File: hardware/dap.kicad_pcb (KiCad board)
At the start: 4 copper layers, 60.8 x 105.8 mm, 158 parts, among them J1 Battery, J2 E-paper FPC, J3 Touch FPC, J4 USB-C, J5 microSD, J6 PJ-342, J7 4.4mm balanced, Q1 Si1308EDL, SW1 Play, SW2 Power, SW3 Vol+, SW4 Vol-, U1 BQ24073RGTR, U10 TUSB320LIRWBR, U11 FSUSB42MUX, U12 GL823K-HCY04, U13 TS3A27518EPWR, U14 SN74AVC4T774PWR, U15 PCA9306DCUR, U16 74LVC1G04, U17 CS43131-CNZR, U18 CS43131-CNZR, U2 TPS63001DRCR, U3 LP5907MFX-1.8, U4 LP5907MFX-1.8, U5 LP5907MFX-1.8, U6 TPS61023DRLR, U7 TPS2553DBVR, U8 ESP32-S3-WROOM-1-N16R8, U9 USBLC6-2SC6, Y1 22.5792MHz, Y2 24.576MHz

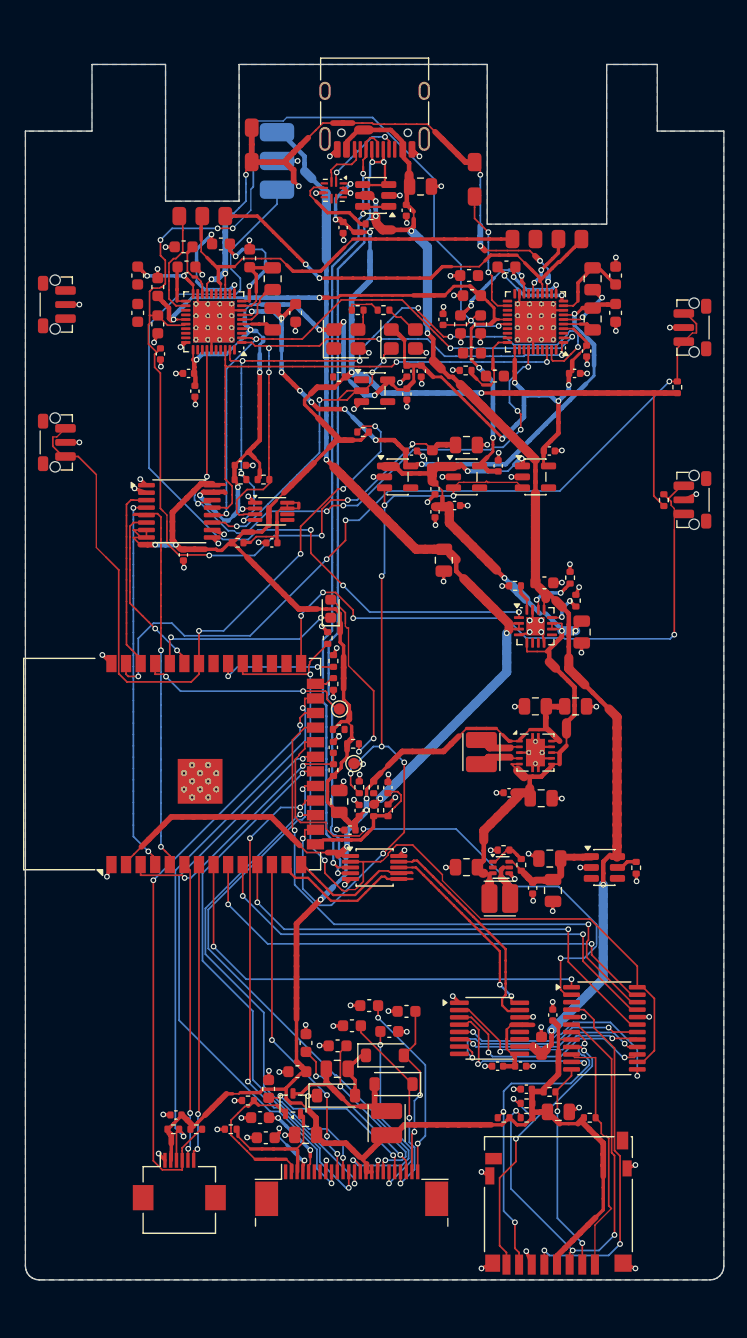
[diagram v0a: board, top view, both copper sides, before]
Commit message: Lengthen the board and case, hang both jacks under the board
The owner moved to a 5000 mAh 806090 cell (8 mm thick), and a 4.4 mm
jack turned out to be about 21 mm deep, not 14. Both headphone jacks now
hang from the back of the board into the top end, where the battery
isn't: the case is 65 x 116 x 17.2 mm and the board 60.8 x 111.8 mm.
Each port's hole is at its own part's height. The case check now also
looks for parts under the board that reach the battery or the back.

Footprints from the parts' drawings: the PJ-342 (SMD, two pegs), the
Kinghelm 4.4 mm jack (12 plated slots, a 1.15 mm notch so its nose ends
inside the case's face, and the cut-out its drawing asks for, with a
keep-out for the routers), and the TF-01A microSD socket. The e-paper
connector moves to x -0.4 mm, centred on the panel's ribbon as measured
on Good Display's drawing. The microSD moves to x 18.5 mm.

Routing is not finished: 32 connections are left in the audio area. The
clocks, level shifters and 1.8 V regulators now sit between the DACs, the
DACs keep a 1.4 mm ring free for their pins, Freerouting may also use
layer 3 (kept free under the USB pairs) and may redo all but the critical
nets, and its log, input and output are kept for another try.
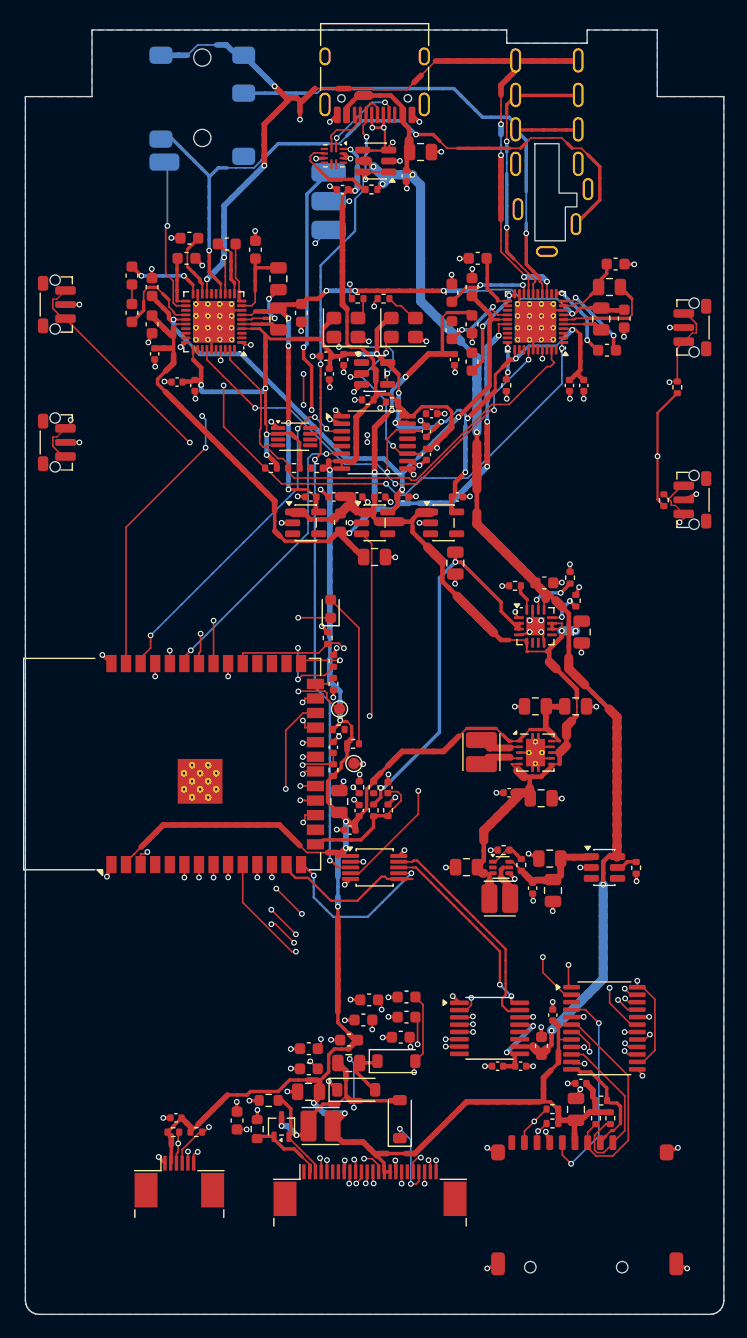
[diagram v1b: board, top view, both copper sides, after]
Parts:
- removed C79: 2.2uF, Capacitor_SMD:C_0603_1608Metric
- C34: value 1uF/50V -> 1uF; footprint Capacitor_SMD:C_0603_1608Metric -> Capacitor_SMD:C_0402_1005Metric
- C35: value 1uF -> 10uF; footprint Capacitor_SMD:C_0402_1005Metric -> Capacitor_SMD:C_0805_2012Metric
- C36, C44: value 10uF -> 100nF; footprint Capacitor_SMD:C_0805_2012Metric -> Capacitor_SMD:C_0402_1005Metric
- C39, C54, C68: value 100nF -> 4.7uF; footprint Capacitor_SMD:C_0402_1005Metric -> Capacitor_SMD:C_0603_1608Metric
- C40: value 4.7uF -> 1uF; footprint Capacitor_SMD:C_0603_1608Metric -> Capacitor_SMD:C_0402_1005Metric
- C41: value 1uF -> 100nF
- C43: value 100nF -> 10uF; footprint Capacitor_SMD:C_0402_1005Metric -> Capacitor_SMD:C_0805_2012Metric
- C55, C69: value 4.7uF -> 2.2uF
- C56, C70: value 2.2uF -> 22uF; footprint Capacitor_SMD:C_0603_1608Metric -> Capacitor_SMD:C_0805_2012Metric
- C57, C71: value 15uF -> 22uF
- C58, C72: value 15uF -> 2.2uF; footprint Capacitor_SMD:C_0805_2012Metric -> Capacitor_SMD:C_0603_1608Metric
- C65: value 2.2uF -> 100nF; footprint Capacitor_SMD:C_0603_1608Metric -> Capacitor_SMD:C_0402_1005Metric
- J3: footprint Connector_FFC-FPC:Hirose_FH12-6S-0.5SH_1x06-1MP_P0.50mm_Horizontal -> Connector_FFC-FPC:Jushuo_AFC07-S06FCA-00_1x6-1MP_P0.50_Horizontal
- J5: footprint Connector_Card:microSD_HC_Hirose_DM3D-SF -> dap:microSD_TF-01A
- J6: footprint dap:Jack_3.5mm_PJ-342_standin -> dap:Jack_3.5mm_PJ-342; moved to B.Cu
- J7: value 4.4mm balanced -> KH-PJ-44002-12DBAP-A; footprint dap:Jack_4.4mm_standin -> dap:Jack_4.4mm_KH-PJ-44002-12DBAP-A; moved to B.Cu
- R21: value 10k -> 1M; footprint Resistor_SMD:R_0402_1005Metric -> Resistor_SMD:R_0603_1608Metric
- R22: footprint Resistor_SMD:R_0402_1005Metric -> Resistor_SMD:R_0603_1608Metric
- R6: value 49.9k -> 47k
- moved C35 86.5 mm to (152.5, 59.7), turned to 0 degrees
- moved C45 55.9 mm to (153.0, 86.0), turned to -90 degrees
- moved C38 52.5 mm to (146.4, 118.7), turned to 180 degrees
- moved C65 38.8 mm to (165.5, 80.0), turned to -90 degrees
- moved C39 25.1 mm to (163.0, 137.5), turned to 90 degrees
- moved C46 23.7 mm to (153.0, 84.0), turned to 90 degrees
- moved C34 19.5 mm to (131.2, 143.8)
- moved C51 18.5 mm to (132.9, 80.0)
- moved U14 18.0 mm to (148.5, 85.0)
- moved C47 17.2 mm to (153.5, 82.5)
- moved C48 17.1 mm to (145.8, 77.8), turned to -90 degrees
- moved C14 12.6 mm to (148.5, 95.0)
- moved C55 12.5 mm to (142.1, 73.7)
- moved C69 12.5 mm to (170.2, 74.2)
- moved C67 11.5 mm to (155.5, 77.8)
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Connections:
- C29 pad 1: /Display/EPD_VPP -> /Display/EPD_VSH
- C30 pad 1: /Display/EPD_VSH -> /Display/EPD_PREVGH
- C31 pad 1: /Display/EPD_PREVGH -> /Display/EPD_VSL
- C32 pad 1: /Display/EPD_VSL -> /Display/EPD_PREVGL
- C33 pad 1: /Display/EPD_PREVGL -> /Display/EPD_VCOM
- C34 pad 1: /Display/EPD_VCOM -> +3V3
- C35 pad 1: +3V3 -> VBUS
- C37 pad 1: VBUS -> +3V3
- C39 pad 1: +3V3 -> VBUS
- C40 pad 1: VBUS -> GL_3V3
- C42 pad 1: GL_3V3 -> +3V3
- C46 pad 1: +3V3 -> 1V8_D
- C47 pad 1: 1V8_D -> /Audio/I2C_VREF2
- C48 pad 1: /Audio/I2C_VREF2 -> 1V8_D
- C53 pad 1: 1V8_D -> VP
- C55 pad 1: VP -> 1V8_A
- C56 pad 1: 1V8_A -> /Audio/DACL_FILTP
- C56 pad 2: GND -> 1V8_A
- C57 pad 1: /Audio/DACL_FILTP -> /Audio/DACL_FILTN
- C57 pad 2: 1V8_A -> /Audio/DACL_NVA
- C58 pad 1: /Audio/DACL_FILTN -> /Audio/DACL_NVA
- C58 pad 2: /Audio/DACL_NVA -> GND
- C59 pad 1: /Audio/DACL_NVA -> /Audio/DACL_FLYP_VA
- C59 pad 2: GND -> /Audio/DACL_FLYN_VA
- C60 pad 1: /Audio/DACL_FLYP_VA -> 1V8_CP
- C60 pad 2: /Audio/DACL_FLYN_VA -> GND
- C61 pad 1: 1V8_CP -> /Audio/DACL_VCPF_P
- C62 pad 1: /Audio/DACL_VCPF_P -> /Audio/DACL_VCPF_N
- C63 pad 1: /Audio/DACL_VCPF_N -> /Audio/DACL_FLYP_VCP
- C63 pad 2: GND -> /Audio/DACL_FLYC_VCP
- C64 pad 1: /Audio/DACL_FLYP_VCP -> /Audio/DACL_FLYC_VCP
- C64 pad 2: /Audio/DACL_FLYC_VCP -> /Audio/DACL_FLYN_VCP
- C65 pad 1: /Audio/DACL_FLYC_VCP -> 1V8_D
- C65 pad 2: /Audio/DACL_FLYN_VCP -> GND
- C67 pad 1: 1V8_D -> VP
- C69 pad 1: VP -> 1V8_A
- C70 pad 1: 1V8_A -> /Audio/DACR_FILTP
- C70 pad 2: GND -> 1V8_A
- C71 pad 1: /Audio/DACR_FILTP -> /Audio/DACR_FILTN
- C71 pad 2: 1V8_A -> /Audio/DACR_NVA
- C72 pad 1: /Audio/DACR_FILTN -> /Audio/DACR_NVA
- C72 pad 2: /Audio/DACR_NVA -> GND
- C73 pad 1: /Audio/DACR_NVA -> /Audio/DACR_FLYP_VA
- C73 pad 2: GND -> /Audio/DACR_FLYN_VA
- C74 pad 1: /Audio/DACR_FLYP_VA -> 1V8_CP
- C74 pad 2: /Audio/DACR_FLYN_VA -> GND
- C75 pad 1: 1V8_CP -> /Audio/DACR_VCPF_P
- C76 pad 1: /Audio/DACR_VCPF_P -> /Audio/DACR_VCPF_N
- C77 pad 1: /Audio/DACR_VCPF_N -> /Audio/DACR_FLYP_VCP
- C77 pad 2: GND -> /Audio/DACR_FLYC_VCP
- C78 pad 1: /Audio/DACR_FLYP_VCP -> /Audio/DACR_FLYC_VCP
- C78 pad 2: /Audio/DACR_FLYC_VCP -> /Audio/DACR_FLYN_VCP
- J2 pad 19: /Display/EPD_VPP -> unconnected-(J2-Pin_19-Pad19)
- J6 pad 3: /Audio/OUT_RP -> /Audio/OUT_LP
- J6 pad 4: /Audio/OUT_LP -> /Audio/DET_35
- J6 pad 5: /Audio/DET_35 -> /Audio/HP_GND
- J7 pad 1: /Audio/OUT_LP -> /Audio/HP_GND
- J7 pad 2: /Audio/OUT_LN -> /Audio/OUT_RN
- J7 pad 4: /Audio/OUT_RN -> /Audio/OUT_LN
- J7 pad 5: /Audio/HP_GND -> /Audio/OUT_LP
- J7 pad 6: /Audio/DET_44 -> /Audio/HP_GND
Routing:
- net /MCU/KEY_VOLUP: track 0.00 -> 55.3 mm, vias 0 -> 3
- net /Audio/SDIN_1V8: track 50.8 -> 0.00 mm, vias 4 -> 0
- net AUDIO_EN: track 68.9 -> 23.8 mm, vias 8 -> 2
- net /Audio/LRCK_1V8: track 44.8 -> 0.00 mm, vias 2 -> 0
- net /Audio/MCLK: track 3.05 -> 41.5 mm, vias 0 -> 4
- net +3V3: track 294.3 -> 256.9 mm
- net I2S_SDOUT: track 34.3 -> 0.00 mm, vias 2 -> 0
- net I2S_LRCK: track 33.0 -> 0.00 mm, vias 2 -> 0
- net VP: track 119.4 -> 88.8 mm, vias 9 -> 7
- net /Audio/HP_GND: track 57.0 -> 86.2 mm, vias 7 -> 8
- net /USB and storage/USB_DM: track 74.2 -> 101.7 mm, vias 3 -> 4
- net /Power/BAT_NTC: track 72.3 -> 45.0 mm, vias 3 -> 6
- net /Audio/OUT_LP: track 35.2 -> 60.4 mm, vias 0 -> 2
- net /USB and storage/SDC_CMD: track 41.1 -> 19.2 mm, vias 3 -> 0
- net /Audio/OUT_RN: track 5.67 -> 24.2 mm
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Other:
- board size 60.8 x 105.8 mm -> 60.8 x 111.8 mm
- board text added: "E-ink DAP v0.1 2026-10-31"
- board text removed: "E-ink DAP v0.1 draft 2026-10-26"

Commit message: Route the board on 6 layers
The board is now top, ground, signal, signal, ground, bottom, and every
net is routed with KiCad's DRC clean.

- Our router routes every net. Its search is guided by the true distance
  through free space (Dijkstra over the window), so long connections no
  longer run out of steps.
- Each fine-pitch pin, every FPC connector pin and every ESP32 pin gets an
  escape stub and a via of its own before routing, so nothing can wall it
  in. A pin with no room takes back its neighbours' vias.
- Rip-up is a trial: kept only if fewer connections are left, otherwise
  put back exactly. It may also move neighbouring pins' vias.
- DAC capacitors that sit between two pins of their chip are placed
  first, with a 0.6 mm ring and a free strip at the charge-pump pins.
- Freerouting only adds to our fixed tracks, and is skipped when nothing
  is left. Dead-end removal can no longer cut a connection, and a repair
  step judged by KiCad's own count closes anything still open.
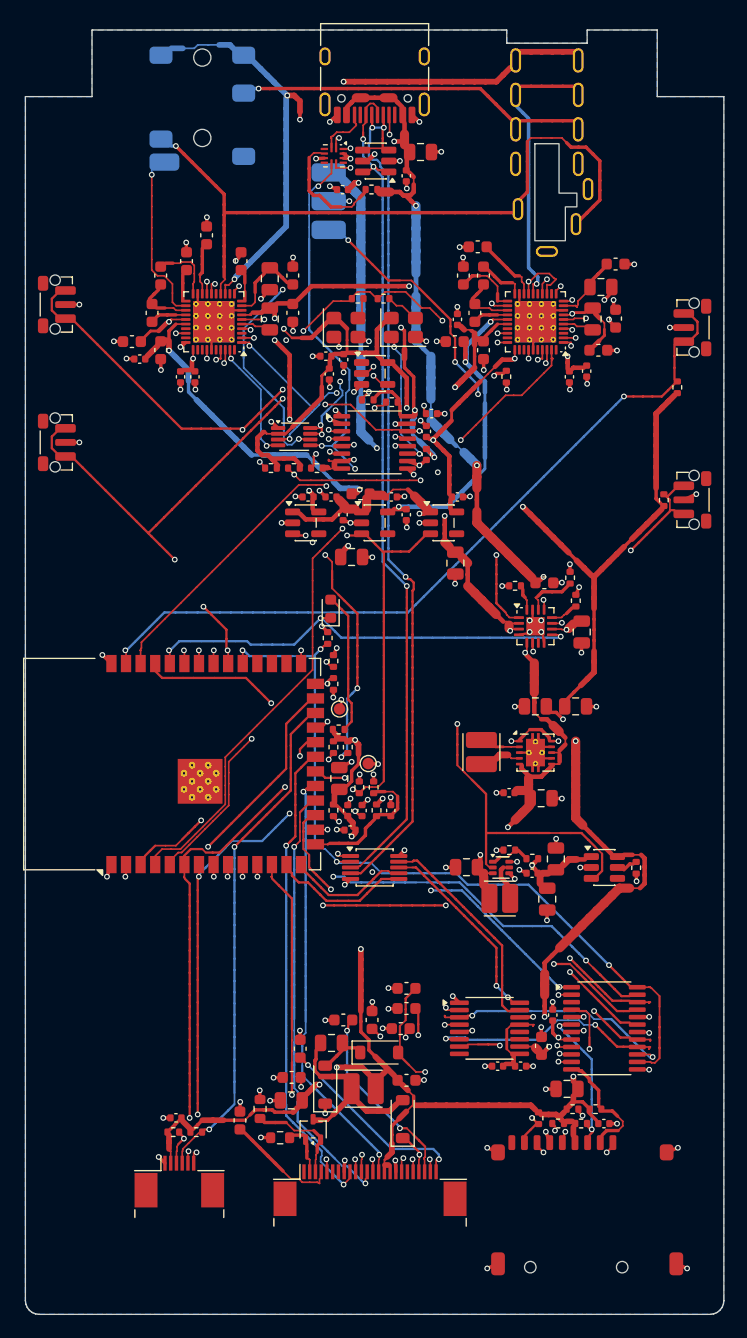
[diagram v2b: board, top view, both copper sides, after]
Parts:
- moved C78 7.57 mm to (158.0, 70.5), turned to 90 degrees
- moved C33 7.35 mm to (142.0, 137.8), turned to 90 degrees
- moved C27 6.10 mm to (151.3, 140.5), turned to 0 degrees
- moved C21 6.04 mm to (147.4, 117.0)
- moved C60 5.06 mm to (127.4, 76.2), turned to 180 degrees
- moved C74 4.98 mm to (155.5, 76.2), turned to 180 degrees
- moved L3 4.96 mm to (147.5, 141.3)
- moved C76 4.59 mm to (157.5, 68.0), turned to 180 degrees
- moved R19 4.16 mm to (146.2, 111.5)
- moved C44 4.03 mm to (168.5, 144.3), turned to 0 degrees
- moved C58 3.95 mm to (141.4, 70.5)
- moved C31 3.91 mm to (145.8, 135.3)
- moved C30 3.88 mm to (151.3, 134.3)
- moved C69 3.55 mm to (168.0, 77.0), turned to 0 degrees
- moved C67 3.51 mm to (155.7, 74.3), turned to 90 degrees
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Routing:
- net I2C_SCL: track 26.3 -> 105.2 mm, vias 2 -> 11
- net I2C_SDA: track 26.1 -> 101.6 mm, vias 2 -> 7
- net DAC_RST: track 14.5 -> 69.5 mm, vias 3 -> 6
- net BOOST_EN: track 1.77 -> 51.5 mm, vias 0 -> 3
- net I2S_LRCK: track 0.00 -> 45.5 mm, vias 0 -> 2
- net I2S_SDOUT: track 0.00 -> 42.8 mm, vias 0 -> 2
- net /Audio/SDIN_1V8: track 0.00 -> 38.8 mm, vias 0 -> 3
- net /Audio/OUT_LN: track 0.00 -> 37.1 mm, vias 0 -> 1
- net /Audio/LRCK_1V8: track 0.00 -> 35.4 mm, vias 0 -> 3
- net +3V3: track 256.9 -> 225.3 mm, vias 11 -> 19
- net VP: track 88.8 -> 58.8 mm, vias 7 -> 5
- net /USB and storage/USB_DM: track 101.7 -> 74.6 mm, vias 4 -> 3
- net CHG_N: track 16.3 -> 38.1 mm, vias 2 -> 3
- net /Audio/I2C_VREF2: track 0.00 -> 18.7 mm, vias 0 -> 5
- net /Audio/DET_44: track 0.00 -> 16.9 mm, vias 0 -> 1
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- added copper zone on In3.Cu, net GND
- added copper zone on In4.Cu, net GND
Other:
- copper layers 4 -> 6
